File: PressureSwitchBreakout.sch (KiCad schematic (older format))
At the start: 3 parts, among them J1 TEST, J2 PCM, SW1 TEST

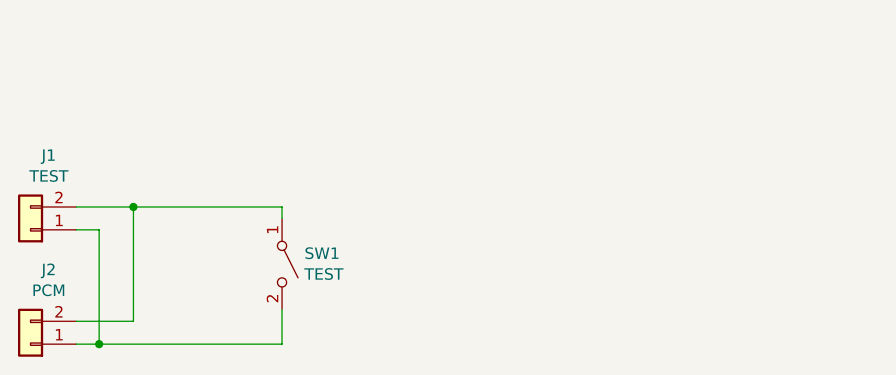
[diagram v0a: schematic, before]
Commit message: Update to kicad 6.0 export gerbers panelize using kikit
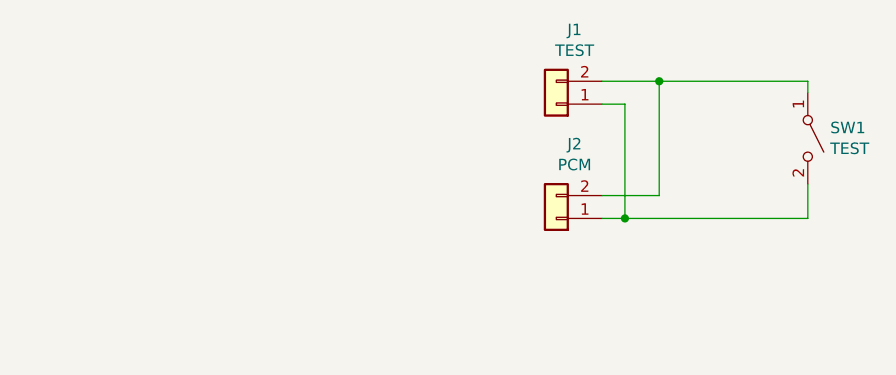
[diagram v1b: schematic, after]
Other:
- moved on the sheet: J1, J2, SW1
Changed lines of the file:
@@
 EESchema Schematic File Version 4
-EELAYER 26 0
+EELAYER 30 0
 EELAYER END
 $Descr A4 11693 8268
 encoding utf-8
 Sheet 1 1
-Title ""
-Date ""
-Rev ""
-Comp ""
+Title "PRESSer"
+Date "2021-12-28"
+Rev "01"
+Comp "FRC2168"
 Comment1 ""
 Comment2 ""
@@
 L Connector_Generic:Conn_01x02 J2
 U 1 1 5C27DD4F
-P 3000 4650
-F 0 "J2" H 2920 4325 50  0000 C CNN
-F 1 "PCM" H 2920 4416 50  0000 C CNN
-F 2 "Connector_PinSocket_2.54mm:PinSocket_1x02_P2.54mm_Vertical" H 3000 4650 50  0001 C CNN
-F 3 "~" H 3000 4650 50  0001 C CNN
-	1    3000 4650
+P 5300 4100
+F 0 "J2" H 5220 3775 50  0000 C CNN
+F 1 "PCM" H 5220 3866 50  0000 C CNN
+F 2 "Connector_PinSocket_2.54mm:PinSocket_1x02_P2.54mm_Vertical" H 5300 4100 50  0001 C CNN
+F 3 "~" H 5300 4100 50  0001 C CNN
+	1    5300 4100
 	-1   0    0    1
 $EndComp
@@
 L Connector_Generic:Conn_01x02 J1
 U 1 1 5C27DFAF
-P 3000 4150
-F 0 "J1" H 2920 3825 50  0000 C CNN
-F 1 "TEST" H 2920 3916 50  0000 C CNN
-F 2 "Connector_PinSocket_2.54mm:PinSocket_1x02_P2.54mm_Vertical" H 3000 4150 50  0001 C CNN
-F 3 "~" H 3000 4150 50  0001 C CNN
-	1    3000 4150
+P 5300 3600
+F 0 "J1" H 5220 3275 50  0000 C CNN
+F 1 "TEST" H 5220 3366 50  0000 C CNN
+F 2 "Connector_PinSocket_2.54mm:PinSocket_1x02_P2.54mm_Vertical" H 5300 3600 50  0001 C CNN
+F 3 "~" H 5300 3600 50  0001 C CNN
+	1    5300 3600
 	-1   0    0    1
 $EndComp
 Wire Wire Line
-	3200 4050 3450 4050
+	5500 3500 5750 3500
 Wire Wire Line
-	3200 4550 3450 4550
+	5500 4000 5750 4000
 Wire Wire Line
-	3450 4550 3450 4050
+	5750 4000 5750 3500
 Wire Wire Line
-	4100 4050 4100 4100
-Connection ~ 3450 4050
+	6400 3500 6400 3550
+Connection ~ 5750 3500
 Wire Wire Line
-	4100 4500 4100 4650
+	6400 3950 6400 4100
 Wire Wire Line
-	3200 4150 3300 4150
+	5500 3600 5600 3600
 Wire Wire Line
-	3300 4150 3300 4650
-Connection ~ 3300 4650
+	5600 3600 5600 4100
+Connection ~ 5600 4100
 Wire Wire Line
-	3300 4650 3200 4650
+	5600 4100 5500 4100
 Wire Wire Line
-	3450 4050 4100 4050
+	5750 3500 6400 3500
 Wire Wire Line
-	3300 4650 4100 4650
+	5600 4100 6400 4100
 $Comp
 L Switch:SW_SPST SW1
 U 1 1 5C27F20D
-P 4100 4300
-F 0 "SW1" V 4054 4398 50  0000 L CNN
-F 1 "TEST" V 4145 4398 50  0000 L CNN
-F 2 "Button_Switch_SMD:SW_SPST_EVQQ2" H 4100 4300 50  0001 C CNN
-F 3 "" H 4100 4300 50  0001 C CNN
-	1    4100 4300
+P 6400 3750
+F 0 "SW1" V 6354 3848 50  0000 L CNN
+F 1 "TEST" V 6445 3848 50  0000 L CNN
+F 2 "Button_Switch_SMD:SW_SPST_EVQQ2" H 6400 3750 50  0001 C CNN
+F 3 "" H 6400 3750 50  0001 C CNN
+	1    6400 3750
 	0    1    1    0
 $EndComp
